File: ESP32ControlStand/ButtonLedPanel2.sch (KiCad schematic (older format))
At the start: 24 parts, among them P201 CONN_5, SW201 SW_PUSH_SMALL, SW202 SW_PUSH_SMALL, SW203 SW_PUSH_SMALL, SW204 SW_PUSH_SMALL, SW205 SW_PUSH_SMALL, SW206 SW_PUSH_SMALL, SW207 SW_PUSH_SMALL, SW208 SW_PUSH_SMALL, T201 Buttons, T202 LEDS, U201 MCP23017, U202 TBD62083A

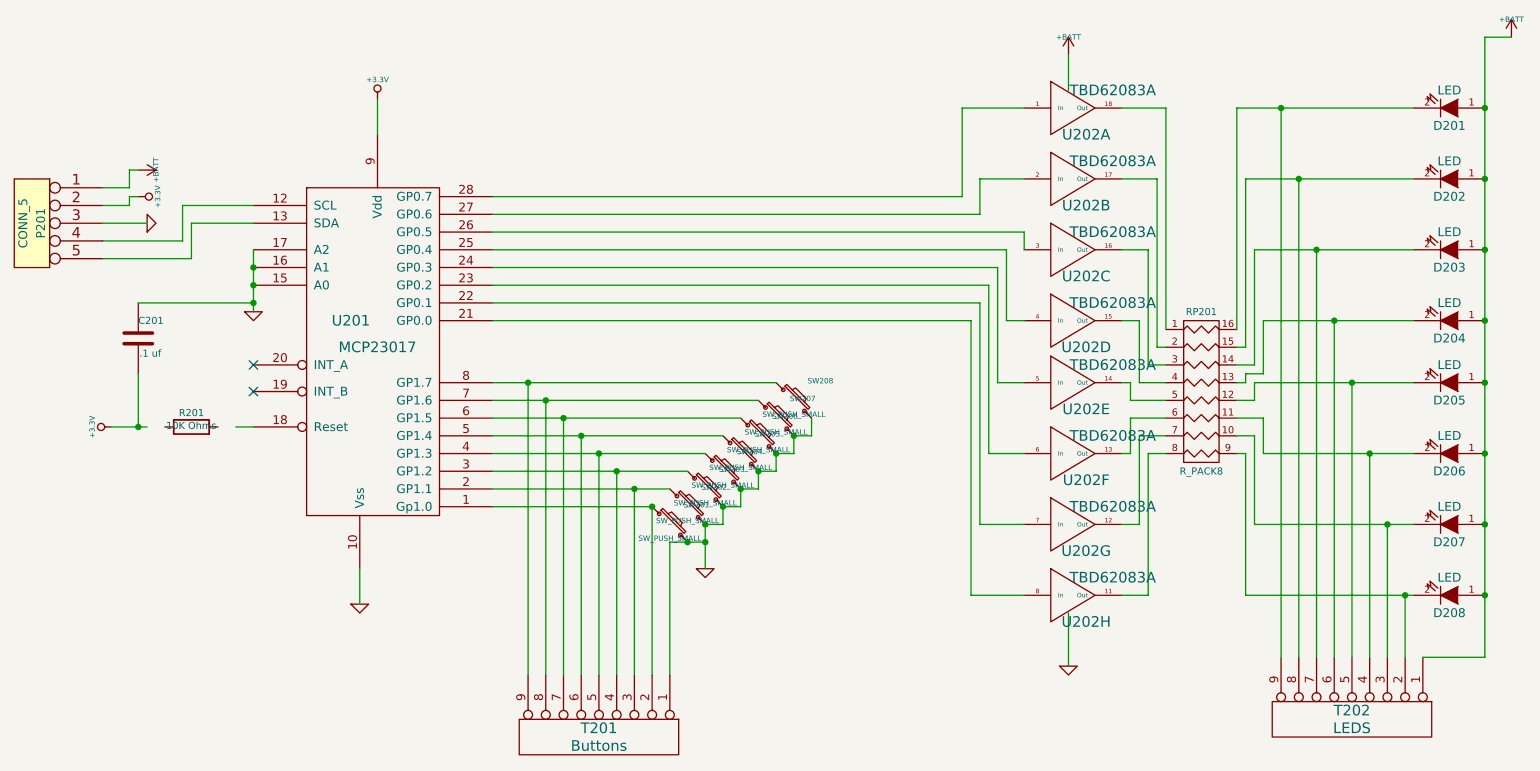
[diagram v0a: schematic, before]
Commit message: Completed first draft of PCBs for ESP32ControlStand.
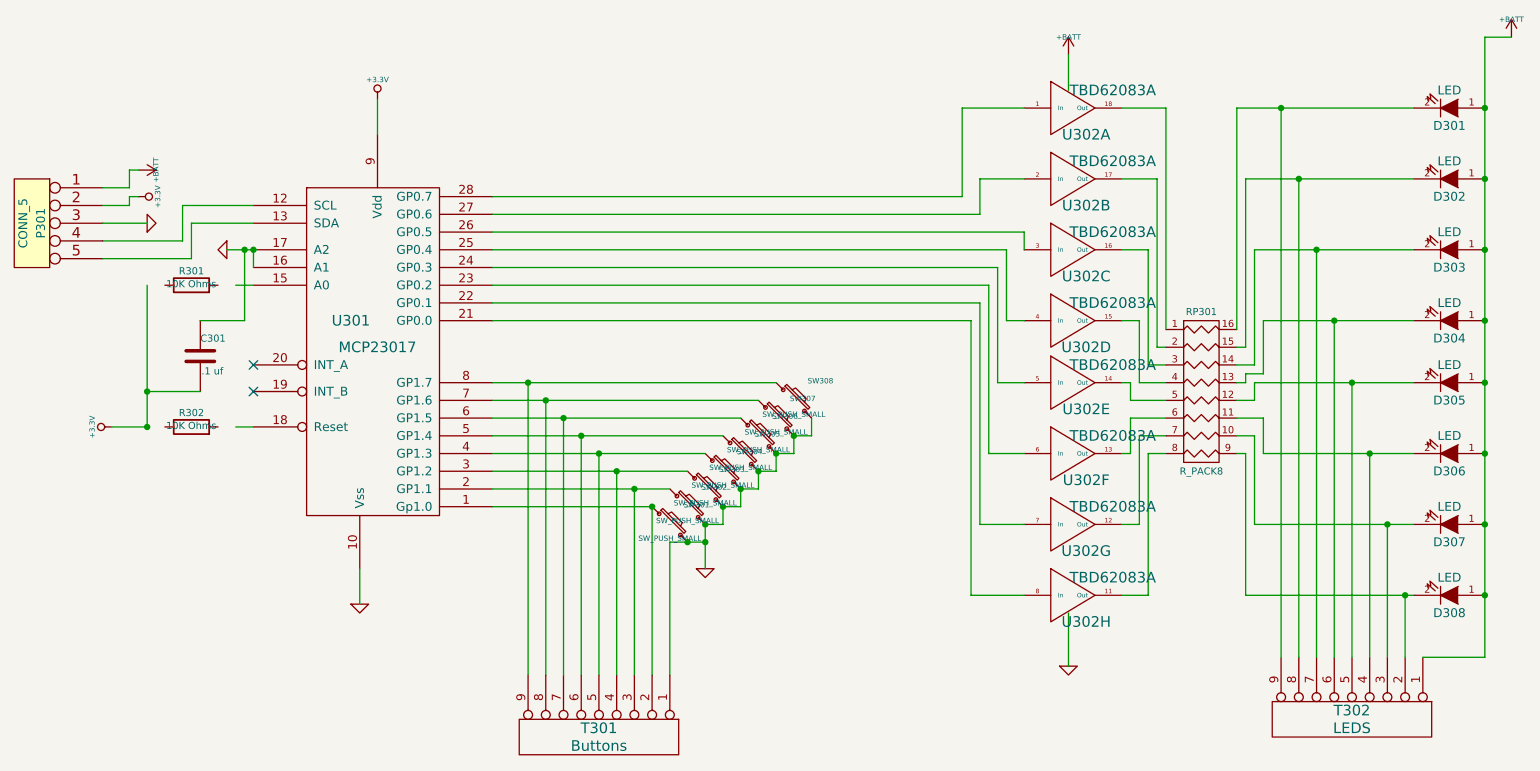
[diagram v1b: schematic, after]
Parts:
- removed C201: .1 uf, ~, symbol C
- removed D201, D202, D203, D204, D205, D206, D207, D208: LED, ~, symbol LED
- removed P201: CONN_5, ~, symbol CONN_5
- removed R201: 10K Ohms, ~, symbol R
- removed RP201: R_PACK8, ~, symbol R_PACK8
- removed SW201, SW202, SW203, SW204, SW205, SW206, SW207, SW208: SW_PUSH_SMALL, ~, symbol SW_PUSH_SMALL
- removed T201: Buttons, ~, symbol CONN_9
- removed T202: LEDS, ~, symbol CONN_9
- removed U201: MCP23017, ~, symbol MCP23017
- removed U202: TBD62083A, ~, symbol TBD62083A
- added C301: .1 uf, ~, symbol C
- added D301, D302, D303, D304, D305, D306, D307, D308: LED, ~, symbol LED
- added P301: CONN_5, ~, symbol CONN_5
- added R301, R302: 10K Ohms, ~, symbol R
- added RP301: R_PACK8, ~, symbol R_PACK8
- added SW301, SW302, SW303, SW304, SW305, SW306, SW307, SW308: SW_PUSH_SMALL, ~, symbol SW_PUSH_SMALL
- added T301: Buttons, ~, symbol CONN_9
- added T302: LEDS, ~, symbol CONN_9
- added U301: MCP23017, ~, symbol MCP23017
- added U302: TBD62083A, ~, symbol TBD62083A
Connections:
- net +3.3V: now also C301.2, P301.2, U301.9 (Vdd)
- net +BATT: now also D301.1 (A), D302.1 (A), D303.1 (A), D304.1 (A), D305.1 (A), D306.1 (A), D307.1 (A), D308.1 (A), P301.1, T302.1 (P1), U302.10 (OC)
- net GND: now also C301.1, P301.3, SW301.2, SW302.2, SW303.2, SW304.2, SW305.2, SW306.2, SW307.2, SW308.2, T301.1 (P1), U301.10 (Vss), U301.16 (A1), U301.17 (A2), U302.9 (IC)
- new net: SW301.1, T301.2 (P2), U301.1 (Gp1.0)
- new net: P301.4, U301.12 (SCL)
- new net: P301.5, U301.13 (SDA)
- new net: SW302.1, T301.3 (P3), U301.2 (GP1.1)
- new net: U301.21 (GP0.0), U302.8 (In)
- new net: U301.22 (GP0.1), U302.7 (In)
- new net: U301.23 (GP0.2), U302.6 (In)
- new net: U301.24 (GP0.3), U302.5 (In)
- new net: U301.25 (GP0.4), U302.4 (In)
- new net: U301.26 (GP0.5), U302.3 (In)
- new net: U301.27 (GP0.6), U302.2 (In)
- new net: U301.28 (GP0.7), U302.1 (In)
- new net: SW303.1, T301.4 (P4), U301.3 (GP1.2)
- new net: SW304.1, T301.5 (P5), U301.4 (GP1.3)
- new net: SW305.1, T301.6 (P6), U301.5 (GP1.4)
- new net: SW306.1, T301.7 (P7), U301.6 (GP1.5)
- new net: SW307.1, T301.8 (P8), U301.7 (GP1.6)
- new net: SW308.1, T301.9 (P9), U301.8 (GP1.7)
- new net: RP301.1 (P1), U302.18 (Out)
- new net: RP301.2 (P2), U302.17 (Out)
- new net: RP301.3 (P3), U302.16 (Out)
- new net: RP301.4 (P4), U302.15 (Out)
- new net: RP301.5 (P5), U302.14 (Out)
- new net: RP301.6 (P6), U302.13 (Out)
- new net: RP301.7 (P7), U302.12 (Out)
- new net: RP301.8 (P8), U302.11 (Out)
- new net: D301.2 (K), RP301.16 (R1), T302.9 (P9)
- new net: D302.2 (K), RP301.15 (R2), T302.8 (P8)
- new net: D303.2 (K), RP301.14 (R3), T302.7 (P7)
- new net: D304.2 (K), RP301.13 (R4), T302.6 (P6)
- new net: D305.2 (K), RP301.12 (R5), T302.5 (P5)
- new net: D306.2 (K), RP301.11 (R6), T302.4 (P4)
- new net: D307.2 (K), RP301.10 (R7), T302.3 (P3)
- new net: D308.2 (K), RP301.9 (R8), T302.2 (P2)

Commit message: Continue FreeCAD work
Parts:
- C301: symbol C -> C-RESCUE-ESP32ControlStand
- D301, D302, D303, D304, D305, D306, D307, D308: symbol LED -> LED-RESCUE-ESP32ControlStand
- R301, R302: symbol R -> R-RESCUE-ESP32ControlStand
- U301: symbol MCP23017 -> MCP23017-RESCUE-ESP32ControlStand
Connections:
- net +3.3V: now also R301.1, R302.1
- net at U301.15 (A0): now also R301.2
- net at U301.18 (Reset): now also R302.2
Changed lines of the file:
@@
 EESchema Schematic File Version 2
+LIBS:ESP32ControlStand-rescue
 LIBS:power
 LIBS:device
@@
 LIBS:memory
 LIBS:xilinx
-LIBS:special
 LIBS:microcontrollers
 LIBS:dsp
@@
 LIBS:adafruit_powerboost_500
 LIBS:ESP32ControlStand-cache
-EELAYER 27 0
+EELAYER 25 0
 EELAYER END
 $Descr A4 11693 8268
@@
 $EndDescr
 $Comp
-L MCP23017 U301
+L MCP23017-RESCUE-ESP32ControlStand U301
 U 1 1 5D94A1AD
 P 4100 2400
@@
 	5950 3400 5950 3650
 $Comp
-L GND #PWR035
+L GND-RESCUE-ESP32ControlStand #PWR035
 U 1 1 5D94A1BE
 P 5950 3650
@@
 Connection ~ 5950 3500
 $Comp
-L LED D301
+L LED-RESCUE-ESP32ControlStand D301
 U 1 1 5D94A1BF
 P 10150 1050
@@
 $EndComp
 $Comp
-L LED D302
+L LED-RESCUE-ESP32ControlStand D302
 U 1 1 5D94A1C0
 P 10150 1450
@@
 $EndComp
 $Comp
-L LED D303
+L LED-RESCUE-ESP32ControlStand D303
 U 1 1 5D94A1C1
 P 10150 1850
@@
 $EndComp
 $Comp
-L LED D304
+L LED-RESCUE-ESP32ControlStand D304
 U 1 1 5D94A1C2
 P 10150 2250
@@
 $EndComp
 $Comp
-L LED D305
+L LED-RESCUE-ESP32ControlStand D305
 U 1 1 5D94A1C3
 P 10150 2600
@@
 $EndComp
 $Comp
-L LED D306
+L LED-RESCUE-ESP32ControlStand D306
 U 1 1 5D94A1C4
 P 10150 3000
@@
 $EndComp
 $Comp
-L LED D307
+L LED-RESCUE-ESP32ControlStand D307
 U 1 1 5D94A1C5
 P 10150 3400
@@
 $EndComp
 $Comp
-L LED D308
+L LED-RESCUE-ESP32ControlStand D308
 U 1 1 5D94A1C6
 P 10150 3800
@@
 $EndComp
 $Comp
-L GND #PWR037
+L GND-RESCUE-ESP32ControlStand #PWR037
 U 1 1 5D94A1C9
 P 8000 4200
@@
 Connection ~ 10350 1050
 $Comp
-L GND #PWR039
+L GND-RESCUE-ESP32ControlStand #PWR039
 U 1 1 5D94A1CB
 P 4000 3850
@@
 	4000 3650 4000 3850
 $Comp
-L +3.3V #PWR040
+L +3.3V-RESCUE-ESP32ControlStand #PWR040
 U 1 1 5D94A1CC
 P 4100 1000
@@
 	4100 1000 4100 1200
 $Comp
-L GND #PWR041
+L GND-RESCUE-ESP32ControlStand #PWR041
 U 1 1 5D94A1CD
 P 3250 1850
@@
 $EndComp
 $Comp
-L R R302
+L R-RESCUE-ESP32ControlStand R302
 U 1 1 5D94A1CE
 P 3050 2850
@@
 $EndComp
 $Comp
-L +3.3V #PWR042
+L +3.3V-RESCUE-ESP32ControlStand #PWR042
 U 1 1 5D94A1CF
 P 2600 2850
@@
 $EndComp
 $Comp
-L +3.3V #PWR044
+L +3.3V-RESCUE-ESP32ControlStand #PWR044
 U 1 1 5D94A1D2
 P 2750 1550
@@
 $EndComp
 $Comp
-L GND #PWR045
+L GND-RESCUE-ESP32ControlStand #PWR045
 U 1 1 5D94A1D3
 P 2800 1700
@@
 	3400 1850 3250 1850
 $Comp
-L R R301
+L R-RESCUE-ESP32ControlStand R301
 U 1 1 5D94D820
 P 3050 2050
@@
 NoConn ~ 3400 2650
 $Comp
-L C C301
+L C-RESCUE-ESP32ControlStand C301
 U 1 1 5D95E29A
 P 3100 2450
